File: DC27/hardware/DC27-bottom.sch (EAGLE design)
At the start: 87 parts, among them IC2 LDL112D33R, IC3 FT2232HL-REEL, IC4 93LC46BT-I_OT, J2 JTAG, J3 Battery, J4 Program Port, U2 ESP-WROOM-32, Y1 ABM7-12.000MHZ-D2Y-T

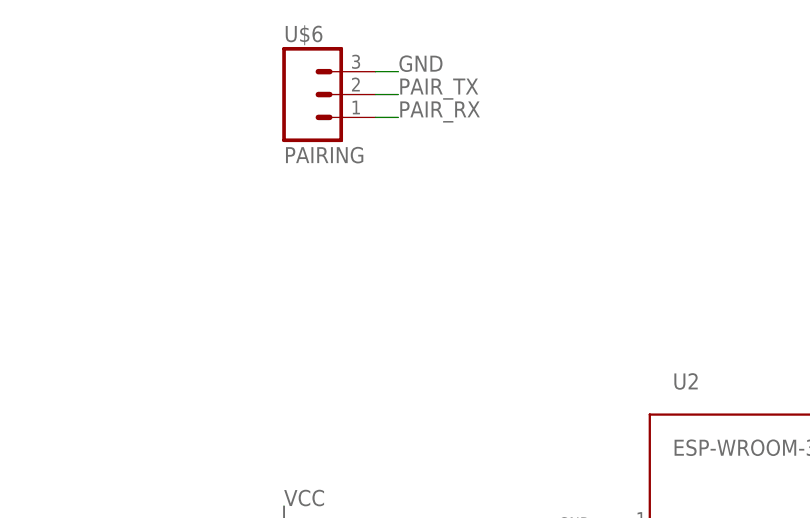
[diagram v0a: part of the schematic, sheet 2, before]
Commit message: moved pairing headers back so they don't stick out
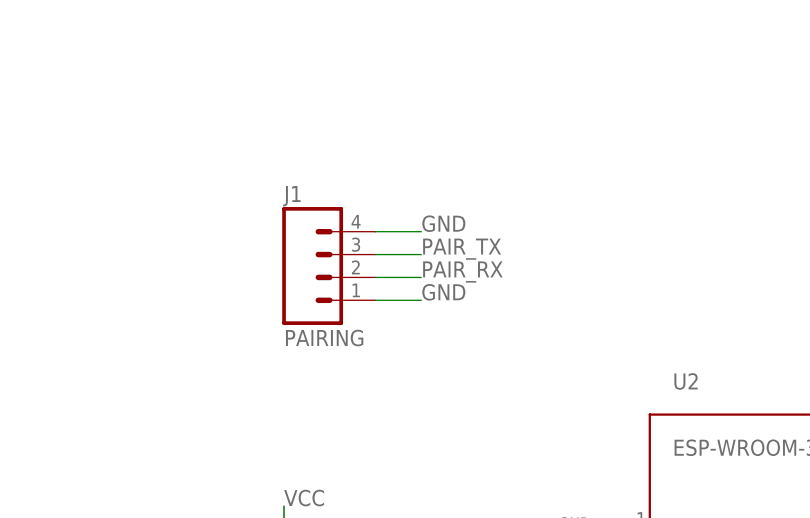
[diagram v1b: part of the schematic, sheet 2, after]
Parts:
- removed U$6: PAIRING, connector:M03PTH
- added J1: PAIRING, connector:M04PTH
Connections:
- net GND: now also J1.1, J1.4; no longer U$6.3
- net PAIR_RX: now also J1.2; no longer U$6.1
- net PAIR_TX: now also J1.3; no longer U$6.2
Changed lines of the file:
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@@
 <part name="R20" library="dc-26" deviceset="RESISTOR" device="0805-RES" value="4.7 K"/>
 <part name="TOP-BOT-CONNECTOR" library="connector" deviceset="M06X2" device=""/>
-<part name="U$6" library="connector" deviceset="M03" device="PTH" value="PAIRING"/>
 <part name="PWR" library="switches" deviceset="MSS3-V-T_R" device=""/>
 <part name="J4" library="connector" deviceset="M06" device="POGO-PIN" value="Program Port"/>
+<part name="J1" library="connector" deviceset="M04" device="PTH" value="PAIRING"/>
 </parts>
 <sheets>
@@
 <attribute name="NAME" x="147.32" y="135.89" size="1.778" layer="95"/>
 </instance>
-<instance part="U$6" gate="J$1" x="50.8" y="137.16" smashed="yes">
-<attribute name="VALUE" x="48.26" y="129.54" size="1.778" layer="96"/>
-<attribute name="NAME" x="48.26" y="143.002" size="1.778" layer="95"/>
-</instance>
 <instance part="J4" gate="G$1" x="27.94" y="12.7" smashed="yes">
 <attribute name="VALUE" x="22.86" y="2.54" size="1.778" layer="96"/>
 <attribute name="NAME" x="22.86" y="23.622" size="1.778" layer="95"/>
+</instance>
+<instance part="J1" gate="G$1" x="53.34" y="116.84" smashed="yes">
+<attribute name="VALUE" x="48.26" y="109.22" size="1.778" layer="96"/>
+<attribute name="NAME" x="48.26" y="125.222" size="1.778" layer="95"/>
 </instance>
 </instances>
@@
 </segment>
 <segment>
-<pinref part="U$6" gate="J$1" pin="3"/>
-<wire x1="58.42" y1="139.7" x2="60.96" y2="139.7" width="0.1524" layer="91"/>
-<label x="60.96" y="139.7" size="1.778" layer="95"/>
-</segment>
-<segment>
 <pinref part="J4" gate="G$1" pin="2"/>
 <wire x1="33.02" y1="10.16" x2="38.1" y2="10.16" width="0.1524" layer="91"/>
 <label x="38.1" y="10.16" size="1.778" layer="95"/>
+</segment>
+<segment>
+<pinref part="J1" gate="G$1" pin="4"/>
+<wire x1="58.42" y1="121.92" x2="63.5" y2="121.92" width="0.1524" layer="91"/>
+<label x="63.5" y="121.92" size="1.778" layer="95"/>
+</segment>
+<segment>
+<pinref part="J1" gate="G$1" pin="1"/>
+<wire x1="58.42" y1="114.3" x2="63.5" y2="114.3" width="0.1524" layer="91"/>
+<label x="63.5" y="114.3" size="1.778" layer="95"/>
 </segment>
 </net>
@@
 </segment>
 <segment>
-<pinref part="U$6" gate="J$1" pin="1"/>
-<wire x1="58.42" y1="134.62" x2="60.96" y2="134.62" width="0.1524" layer="91"/>
-<label x="60.96" y="134.62" size="1.778" layer="95"/>
+<pinref part="J1" gate="G$1" pin="2"/>
+<wire x1="58.42" y1="116.84" x2="63.5" y2="116.84" width="0.1524" layer="91"/>
+<label x="63.5" y="116.84" size="1.778" layer="95"/>
 </segment>
 </net>
@@
 </segment>
 <segment>
-<pinref part="U$6" gate="J$1" pin="2"/>
-<wire x1="58.42" y1="137.16" x2="60.96" y2="137.16" width="0.1524" layer="91"/>
-<label x="60.96" y="137.16" size="1.778" layer="95"/>
-</segment>
-</net>
+<pinref part="J1" gate="G$1" pin="3"/>
+<wire x1="58.42" y1="119.38" x2="63.5" y2="119.38" width="0.1524" layer="91"/>
+<label x="63.5" y="119.38" size="1.778" layer="95"/>
+</segment>
+</net>

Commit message: swaping touch_data_in and touch_data_out
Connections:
- net TOUCH_DATA_IN: now also U2.IO33; no longer U2.IO35
- net TOUCH_DATA_OUT: now also U2.IO35; no longer U2.IO33
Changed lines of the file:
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@@
 <?xml version="1.0" encoding="utf-8"?>
 <!DOCTYPE eagle SYSTEM "eagle.dtd">
-<eagle version="9.4.0">
+<eagle version="9.4.1">
 <drawing>
 <settings>
@@
 <net name="TOUCH_DATA_IN" class="0">
 <segment>
+<pinref part="U$10" gate="G$1" pin="T_DIN"/>
+<wire x1="108.966" y1="-43.18" x2="104.14" y2="-43.18" width="0.1524" layer="91"/>
+<label x="88.9" y="-43.18" size="1.016" layer="95"/>
+</segment>
+<segment>
+<pinref part="U2" gate="G$1" pin="IO33"/>
+<wire x1="86.36" y1="68.58" x2="78.74" y2="68.58" width="0.1524" layer="91"/>
+<label x="63.5" y="68.58" size="1.27" layer="95"/>
+</segment>
+</net>
+<net name="TOUCH_DATA_OUT" class="0">
+<segment>
+<pinref part="U$10" gate="G$1" pin="T_DO"/>
+<wire x1="108.966" y1="-45.72" x2="104.14" y2="-45.72" width="0.1524" layer="91"/>
+<label x="88.9" y="-45.72" size="1.016" layer="95"/>
+</segment>
+<segment>
 <pinref part="U2" gate="G$1" pin="IO35"/>
 <wire x1="86.36" y1="73.66" x2="78.74" y2="73.66" width="0.1524" layer="91"/>
 <label x="63.5" y="73.66" size="1.27" layer="95"/>
 </segment>
-<segment>
-<pinref part="U$10" gate="G$1" pin="T_DIN"/>
-<wire x1="108.966" y1="-43.18" x2="104.14" y2="-43.18" width="0.1524" layer="91"/>
-<label x="88.9" y="-43.18" size="1.016" layer="95"/>
-</segment>
-</net>
-<net name="TOUCH_DATA_OUT" class="0">
-<segment>
-<pinref part="U2" gate="G$1" pin="IO33"/>
-<wire x1="86.36" y1="68.58" x2="78.74" y2="68.58" width="0.1524" layer="91"/>
-<label x="63.5" y="68.58" size="1.27" layer="95"/>
-</segment>
-<segment>
-<pinref part="U$10" gate="G$1" pin="T_DO"/>
-<wire x1="108.966" y1="-45.72" x2="104.14" y2="-45.72" width="0.1524" layer="91"/>
-<label x="88.9" y="-45.72" size="1.016" layer="95"/>
-</segment>
-</net>
+</net>

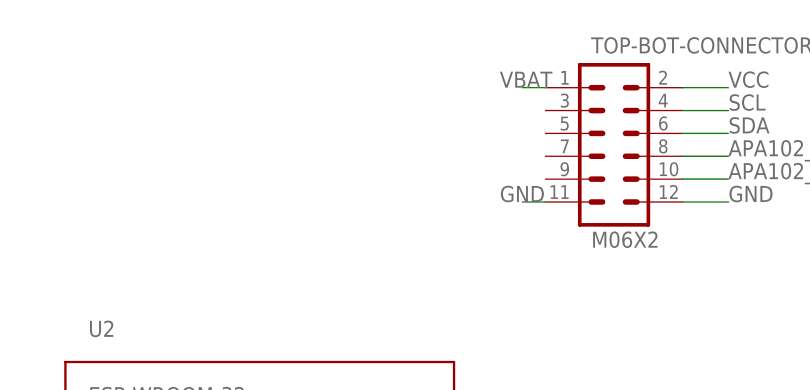
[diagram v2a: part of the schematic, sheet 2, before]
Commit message: Enable line of pwr switch is now what powers vbat on top board, so if you turnoff the badge top the top and the bottom board are off.  :) Increased top board caps to 1206 from 0805
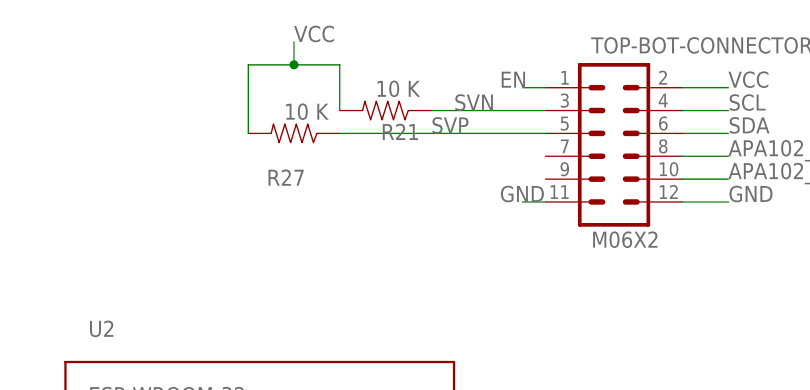
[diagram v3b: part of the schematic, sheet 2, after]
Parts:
- added R21, R27: 10 K, dc-26:RESISTOR0805-RES
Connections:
- net EN: now also TOP-BOT-CONNECTOR.1
- net SVN: now also R21.1, TOP-BOT-CONNECTOR.3
- net SVP: now also R27.1, TOP-BOT-CONNECTOR.5
- net VBAT: no longer TOP-BOT-CONNECTOR.1
- net VCC: now also R21.2, R27.2
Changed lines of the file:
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@@
 <part name="J4" library="connector" deviceset="M06" device="POGO-PIN" value="Program Port"/>
 <part name="J1" library="connector" deviceset="M04" device="PTH" value="PAIRING"/>
+<part name="R21" library="dc-26" deviceset="RESISTOR" device="0805-RES" value="10 K"/>
+<part name="R27" library="dc-26" deviceset="RESISTOR" device="0805-RES" value="10 K"/>
 </parts>
 <sheets>
@@
 <attribute name="NAME" x="48.26" y="125.222" size="1.778" layer="95"/>
 </instance>
+<instance part="R21" gate="G$1" x="124.46" y="129.54" smashed="yes" rot="R180">
+<attribute name="NAME" x="128.27" y="128.0414" size="1.778" layer="95" rot="R180"/>
+<attribute name="VALUE" x="128.27" y="132.842" size="1.778" layer="96" rot="R180"/>
+</instance>
+<instance part="R27" gate="G$1" x="114.3" y="127" smashed="yes" rot="R180">
+<attribute name="NAME" x="115.57" y="122.9614" size="1.778" layer="95" rot="R180"/>
+<attribute name="VALUE" x="118.11" y="130.302" size="1.778" layer="96" rot="R180"/>
+</instance>
 </instances>
 <busses>
@@
 <wire x1="33.02" y1="20.32" x2="38.1" y2="20.32" width="0.1524" layer="91"/>
 <label x="38.1" y="20.32" size="1.778" layer="95"/>
+</segment>
+<segment>
+<pinref part="R21" gate="G$1" pin="2"/>
+<wire x1="119.38" y1="129.54" x2="119.38" y2="134.62" width="0.1524" layer="91"/>
+<pinref part="R27" gate="G$1" pin="2"/>
+<wire x1="109.22" y1="127" x2="109.22" y2="134.62" width="0.1524" layer="91"/>
+<wire x1="119.38" y1="134.62" x2="114.3" y2="134.62" width="0.1524" layer="91"/>
+<wire x1="114.3" y1="134.62" x2="109.22" y2="134.62" width="0.1524" layer="91"/>
+<wire x1="114.3" y1="134.62" x2="114.3" y2="137.16" width="0.1524" layer="91"/>
+<junction x="114.3" y="134.62"/>
+<label x="114.3" y="137.16" size="1.778" layer="95"/>
 </segment>
 </net>
@@
 <label x="76.2" y="81.28" size="1.27" layer="95"/>
 </segment>
+<segment>
+<pinref part="TOP-BOT-CONNECTOR" gate="G$1" pin="5"/>
+<wire x1="142.24" y1="127" x2="119.38" y2="127" width="0.1524" layer="91"/>
+<pinref part="R27" gate="G$1" pin="1"/>
+<label x="129.54" y="127" size="1.778" layer="95"/>
+</segment>
 </net>
 <net name="SVN" class="0">
@@
 <wire x1="86.36" y1="78.74" x2="81.28" y2="78.74" width="0.1524" layer="91"/>
 <label x="76.2" y="78.74" size="1.27" layer="95"/>
+</segment>
+<segment>
+<pinref part="TOP-BOT-CONNECTOR" gate="G$1" pin="3"/>
+<wire x1="142.24" y1="129.54" x2="129.54" y2="129.54" width="0.1524" layer="91"/>
+<pinref part="R21" gate="G$1" pin="1"/>
+<label x="132.08" y="129.54" size="1.778" layer="95"/>
 </segment>
 </net>
@@
 </segment>
 </net>
-<net name="VBAT" class="2">
+<net name="EN" class="0">
 <segment>
 <pinref part="TOP-BOT-CONNECTOR" gate="G$1" pin="1"/>

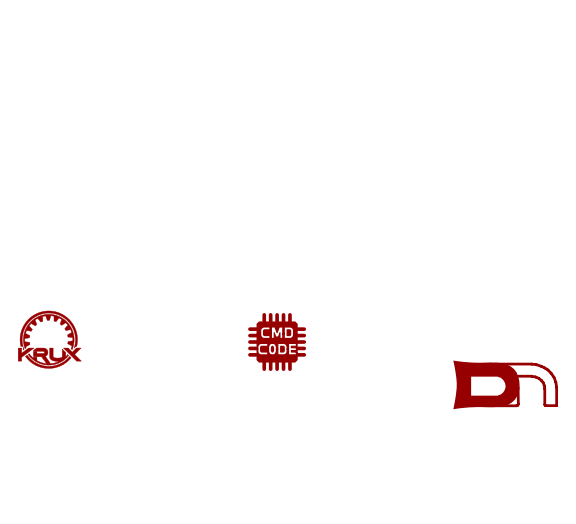
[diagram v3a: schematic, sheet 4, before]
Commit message: Added puzzle elemenets for Krux's Challenge.
Added puzzle elemenets for Krux's Challenge.  Cleaned up size/font/position for part labels
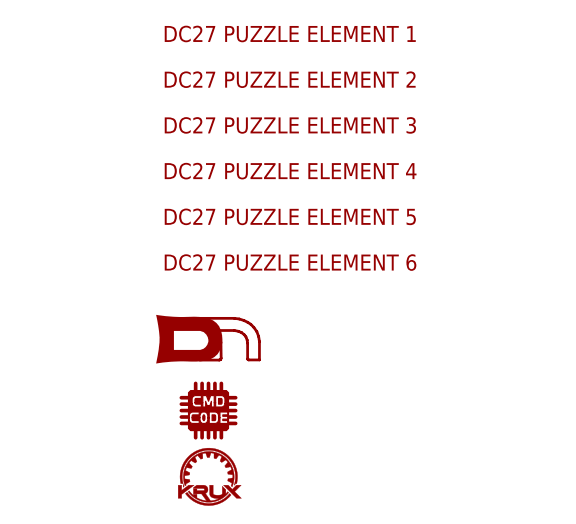
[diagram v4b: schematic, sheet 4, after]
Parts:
- added U$11: DC27_PUZZLE_ELEMENT_2, darknet_parts_library:DC27_PUZZLE_ELEMENT_2
- added U$12: DC27_PUZZLE_ELEMENT_3, darknet_parts_library:DC27_PUZZLE_ELEMENT_3
- added U$13: DC27_PUZZLE_ELEMENT_4, darknet_parts_library:DC27_PUZZLE_ELEMENT_4
- added U$14: DC27_PUZZLE_ELEMENT_5, darknet_parts_library:DC27_PUZZLE_ELEMENT_5
- added U$15: DC27_PUZZLE_ELEMENT_6, darknet_parts_library:DC27_PUZZLE_ELEMENT_6
- added U$6: DC27_PUZZLE_ELEMENT_1, darknet_parts_library:DC27_PUZZLE_ELEMENT_1
- U$7: value KRUX_LOGOKRUX_LOGO_SILK -> KRUX_LOGO; device logos:KRUX_LOGOKRUX_LOGO_SILK -> logos:KRUX_LOGO

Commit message: Fixed the darknet logo, and made resistors pretty
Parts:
- U$9: value DN_LOGO -> DN_LOGODC26; device logos:DN_LOGO -> darknet_parts_library:DN_LOGODC26
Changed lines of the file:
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@@
 <grid distance="0.1" unitdist="inch" unit="inch" style="lines" multiple="1" display="no" altdistance="0.01" altunitdist="inch" altunit="inch"/>
 <layers>
-<layer number="1" name="Top" color="4" fill="1" visible="yes" active="no"/>
-<layer number="2" name="Route2" color="16" fill="1" visible="yes" active="no"/>
-<layer number="3" name="Route3" color="17" fill="1" visible="yes" active="no"/>
-<layer number="4" name="Route4" color="18" fill="1" visible="yes" active="no"/>
-<layer number="5" name="Route5" color="19" fill="1" visible="yes" active="no"/>
-<layer number="6" name="Route6" color="25" fill="1" visible="yes" active="no"/>
-<layer number="7" name="Route7" color="26" fill="1" visible="yes" active="no"/>
-<layer number="8" name="Route8" color="27" fill="1" visible="yes" active="no"/>
-<layer number="9" name="Route9" color="28" fill="1" visible="yes" active="no"/>
-<layer number="10" name="Route10" color="29" fill="1" visible="yes" active="no"/>
-<layer number="11" name="Route11" color="30" fill="1" visible="yes" active="no"/>
-<layer number="12" name="Route12" color="20" fill="1" visible="yes" active="no"/>
-<layer number="13" name="Route13" color="21" fill="1" visible="yes" active="no"/>
-<layer number="14" name="Route14" color="22" fill="1" visible="yes" active="no"/>
-<layer number="15" name="Route15" color="23" fill="1" visible="yes" active="no"/>
-<layer number="16" name="Bottom" color="1" fill="1" visible="yes" active="no"/>
-<layer number="17" name="Pads" color="2" fill="1" visible="yes" active="no"/>
-<layer number="18" name="Vias" color="2" fill="1" visible="yes" active="no"/>
-<layer number="19" name="Unrouted" color="6" fill="1" visible="yes" active="no"/>
-<layer number="20" name="Dimension" color="24" fill="1" visible="yes" active="no"/>
-<layer number="21" name="tPlace" color="7" fill="1" visible="yes" active="no"/>
-<layer number="22" name="bPlace" color="7" fill="1" visible="yes" active="no"/>
-<layer number="23" name="tOrigins" color="15" fill="1" visible="yes" active="no"/>
-<layer number="24" name="bOrigins" color="15" fill="1" visible="yes" active="no"/>
-<layer number="25" name="tNames" color="7" fill="1" visible="yes" active="no"/>
-<layer number="26" name="bNames" color="7" fill="1" visible="yes" active="no"/>
-<layer number="27" name="tValues" color="7" fill="1" visible="yes" active="no"/>
-<layer number="28" name="bValues" color="7" fill="1" visible="yes" active="no"/>
+<layer number="1" name="Top" color="4" fill="1" visible="no" active="no"/>
+<layer number="2" name="Route2" color="16" fill="1" visible="no" active="no"/>
+<layer number="3" name="Route3" color="17" fill="1" visible="no" active="no"/>
+<layer number="4" name="Route4" color="18" fill="1" visible="no" active="no"/>
+<layer number="5" name="Route5" color="19" fill="1" visible="no" active="no"/>
+<layer number="6" name="Route6" color="25" fill="1" visible="no" active="no"/>
+<layer number="7" name="Route7" color="26" fill="1" visible="no" active="no"/>
+<layer number="8" name="Route8" color="27" fill="1" visible="no" active="no"/>
+<layer number="9" name="Route9" color="28" fill="1" visible="no" active="no"/>
+<layer number="10" name="Route10" color="29" fill="1" visible="no" active="no"/>
+<layer number="11" name="Route11" color="30" fill="1" visible="no" active="no"/>
+<layer number="12" name="Route12" color="20" fill="1" visible="no" active="no"/>
+<layer number="13" name="Route13" color="21" fill="1" visible="no" active="no"/>
+<layer number="14" name="Route14" color="22" fill="1" visible="no" active="no"/>
+<layer number="15" name="Route15" color="23" fill="1" visible="no" active="no"/>
+<layer number="16" name="Bottom" color="1" fill="1" visible="no" active="no"/>
+<layer number="17" name="Pads" color="2" fill="1" visible="no" active="no"/>
+<layer number="18" name="Vias" color="2" fill="1" visible="no" active="no"/>
+<layer number="19" name="Unrouted" color="6" fill="1" visible="no" active="no"/>
+<layer number="20" name="Dimension" color="24" fill="1" visible="no" active="no"/>
+<layer number="21" name="tPlace" color="7" fill="1" visible="no" active="no"/>
+<layer number="22" name="bPlace" color="7" fill="1" visible="no" active="no"/>
+<layer number="23" name="tOrigins" color="15" fill="1" visible="no" active="no"/>
+<layer number="24" name="bOrigins" color="15" fill="1" visible="no" active="no"/>
+<layer number="25" name="tNames" color="7" fill="1" visible="no" active="no"/>
+<layer number="26" name="bNames" color="7" fill="1" visible="no" active="no"/>
+<layer number="27" name="tValues" color="7" fill="1" visible="no" active="no"/>
+<layer number="28" name="bValues" color="7" fill="1" visible="no" active="no"/>
 <layer number="29" name="tStop" color="7" fill="3" visible="no" active="no"/>
 <layer number="30" name="bStop" color="7" fill="6" visible="no" active="no"/>
@@
 <layer number="35" name="tGlue" color="7" fill="4" visible="no" active="no"/>
 <layer number="36" name="bGlue" color="7" fill="5" visible="no" active="no"/>
-<layer number="37" name="tTest" color="7" fill="1" visible="yes" active="no"/>
-<layer number="38" name="bTest" color="7" fill="1" visible="yes" active="no"/>
+<layer number="37" name="tTest" color="7" fill="1" visible="no" active="no"/>
+<layer number="38" name="bTest" color="7" fill="1" visible="no" active="no"/>
 <layer number="39" name="tKeepout" color="4" fill="11" visible="no" active="no"/>
 <layer number="40" name="bKeepout" color="1" fill="11" visible="no" active="no"/>
@@
 <layer number="44" name="Drills" color="7" fill="1" visible="no" active="no"/>
 <layer number="45" name="Holes" color="7" fill="1" visible="no" active="no"/>
-<layer number="46" name="Milling" color="3" fill="1" visible="yes" active="no"/>
-<layer number="47" name="Measures" color="7" fill="1" visible="yes" active="no"/>
-<layer number="48" name="Document" color="7" fill="1" visible="yes" active="no"/>
-<layer number="49" name="Reference" color="7" fill="1" visible="yes" active="no"/>
-<layer number="50" name="dxf" color="7" fill="1" visible="yes" active="no"/>
-<layer number="51" name="tDocu" color="7" fill="1" visible="yes" active="no"/>
-<layer number="52" name="bDocu" color="7" fill="1" visible="yes" active="no"/>
-<layer number="53" name="tGND_GNDA" color="7" fill="9" visible="yes" active="no"/>
-<layer number="54" name="bGND_GNDA" color="1" fill="9" visible="yes" active="no"/>
-<layer number="56" name="wert" color="7" fill="1" visible="yes" active="no"/>
-<layer number="57" name="tCAD" color="7" fill="1" visible="yes" active="no"/>
-<layer number="59" name="tCarbon" color="7" fill="1" visible="yes" active="no"/>
-<layer number="60" name="bCarbon" color="7" fill="1" visible="yes" active="no"/>
+<layer number="46" name="Milling" color="3" fill="1" visible="no" active="no"/>
+<layer number="47" name="Measures" color="7" fill="1" visible="no" active="no"/>
+<layer number="48" name="Document" color="7" fill="1" visible="no" active="no"/>
+<layer number="49" name="Reference" color="7" fill="1" visible="no" active="no"/>
+<layer number="50" name="dxf" color="7" fill="1" visible="no" active="no"/>
+<layer number="51" name="tDocu" color="7" fill="1" visible="no" active="no"/>
+<layer number="52" name="bDocu" color="7" fill="1" visible="no" active="no"/>
+<layer number="53" name="tGND_GNDA" color="7" fill="9" visible="no" active="no"/>
+<layer number="54" name="bGND_GNDA" color="1" fill="9" visible="no" active="no"/>
+<layer number="56" name="wert" color="7" fill="1" visible="no" active="no"/>
+<layer number="57" name="tCAD" color="7" fill="1" visible="no" active="no"/>
+<layer number="59" name="tCarbon" color="7" fill="1" visible="no" active="no"/>
+<layer number="60" name="bCarbon" color="7" fill="1" visible="no" active="no"/>
 <layer number="88" name="SimResults" color="9" fill="1" visible="yes" active="yes"/>
 <layer number="89" name="SimProbes" color="9" fill="1" visible="yes" active="yes"/>
@@
 <part name="U$7" library="logos" deviceset="KRUX_LOGO" device="" value="KRUX_LOGO"/>
 <part name="U$8" library="logos" deviceset="CMD_C0DE_LOGO" device="" value="CMD_C0DE_LOGO"/>
-<part name="U$9" library="logos" deviceset="DN_LOGO" device="" value="DN_LOGO"/>
+<part name="U$9" library="darknet_parts_library" deviceset="DN_LOGO" device="DC26" value="DN_LOGODC26"/>
 <part name="U$1" library="connector" deviceset="M06X2" device=""/>
 <part name="R22" library="passives" deviceset="RESISTOR" device="0805-RES" value="10 K"/>
